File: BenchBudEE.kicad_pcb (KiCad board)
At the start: 4 copper layers, 165.1 x 63.5 mm, 54 parts, among them K1 1461069-5, P1 24-pin Mini-Fit Jr., P2 CONN_2, P3 CONN_3X2, P4 12-pin Terminal Block, P5 3-pin TB, Q1 2N3404, U1 LTV-816S, U10 LMT84, U11 OPA4170, U9 MCP3901

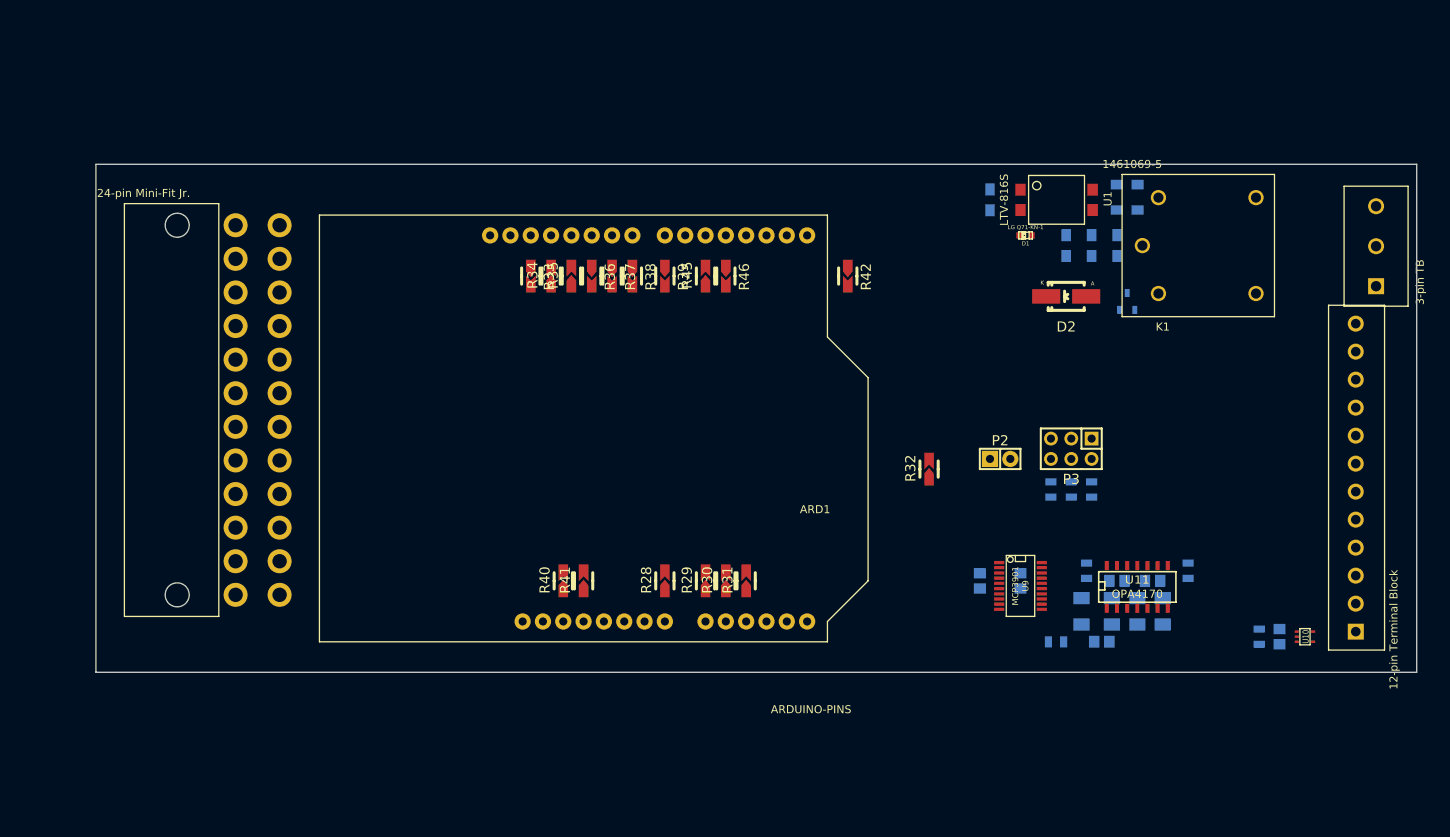
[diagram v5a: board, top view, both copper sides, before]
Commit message: Associated and placed the Current/Fan Driver Module
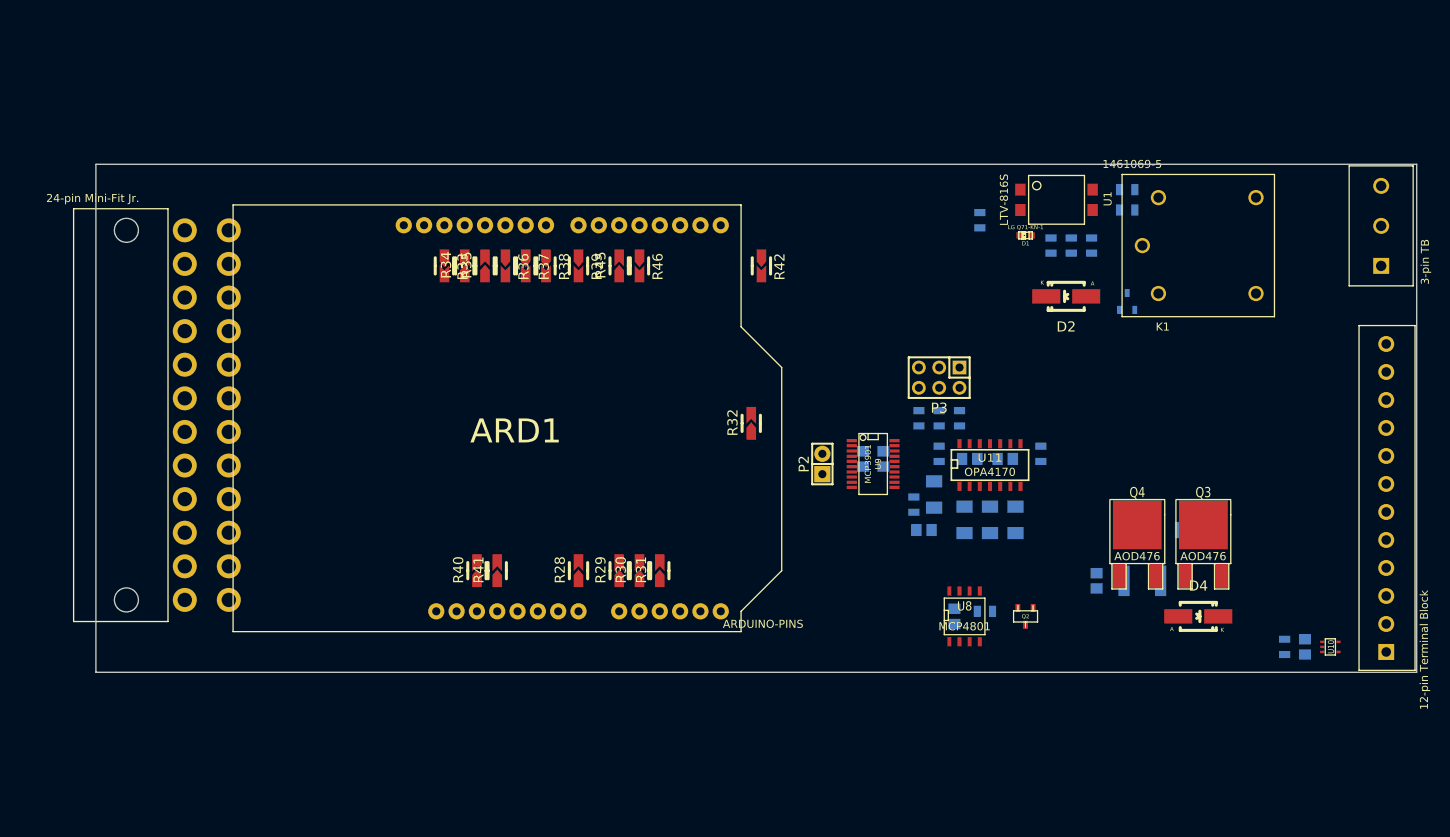
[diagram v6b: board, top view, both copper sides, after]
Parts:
- added C11: C, Capacitors_SMD:c_0805, B.Cu at (236.9, 168.3)
- added C12: C, Capacitors_SMD:c_0805, B.Cu at (254.6, 163.8)
- added D4: B130-13-F, Diodes_SMD:Diode-SMA_Handsoldering, F.Cu at (267.3, 168.3)
- added Q2: DMN65D8L-7, Transistors_SMD:sot23, F.Cu at (245.7, 168.3)
- added Q3: AOD476, SMD_Packages:DPAK2, F.Cu at (268.0, 163.2)
- added Q4: AOD476, SMD_Packages:DPAK2, F.Cu at (259.7, 163.2)
- added R19: R, SMD_Packages:SM0805, B.Cu at (240.7, 167.6)
- added R20: R, SMD_Packages:SM1206, B.Cu at (263.5, 157.5)
- added TH5: MINISMDC050F-2, SMD_Packages:SM1812, B.Cu at (260.4, 163.8)
- added U8: MCP4801, SMD_Packages:SO8N, F.Cu at (238.1, 168.3)
- R1, R2, R3, R4, R5, R6: footprint Resistors_SMD:Resistor_SMD0805_HandSoldering -> SMD_Packages:SM0805
- moved C7 26.3 mm to (233.0, 157.5)
- moved R48 24.7 mm to (231.8, 154.3), turned to 270 degrees
- moved R21 24.4 mm to (238.1, 156.2), turned to 90 degrees
- moved C8 23.9 mm to (238.8, 148.6)
- moved U9 23.9 mm to (226.7, 149.2)
- moved C9 23.9 mm to (243.2, 148.6)
- moved U11 23.9 mm to (241.3, 149.2)
- moved R27 23.5 mm to (234.9, 148.0)
- moved R22 23.5 mm to (234.3, 153.0), turned to 90 degrees
- moved R25 23.5 mm to (247.7, 148.0)
- moved R32 22.9 mm to (211.5, 144.1)
- moved C5 22.9 mm to (228.0, 148.6)
- moved P2 22.2 mm to (220.3, 149.2), turned to 90 degrees
- moved R23 21.7 mm to (244.5, 156.2)
- moved C6 21.1 mm to (225.4, 148.6)
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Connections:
- net /Arduino/ADC_CS_N renamed /Arduino/~ADC_CS
- ARD1 pad 27: (no net) -> Net-(ARD1-Pad27)
- ARD1 pad 28: (no net) -> Net-(ARD1-Pad28)

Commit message: Associated and placed the Power Filter Module
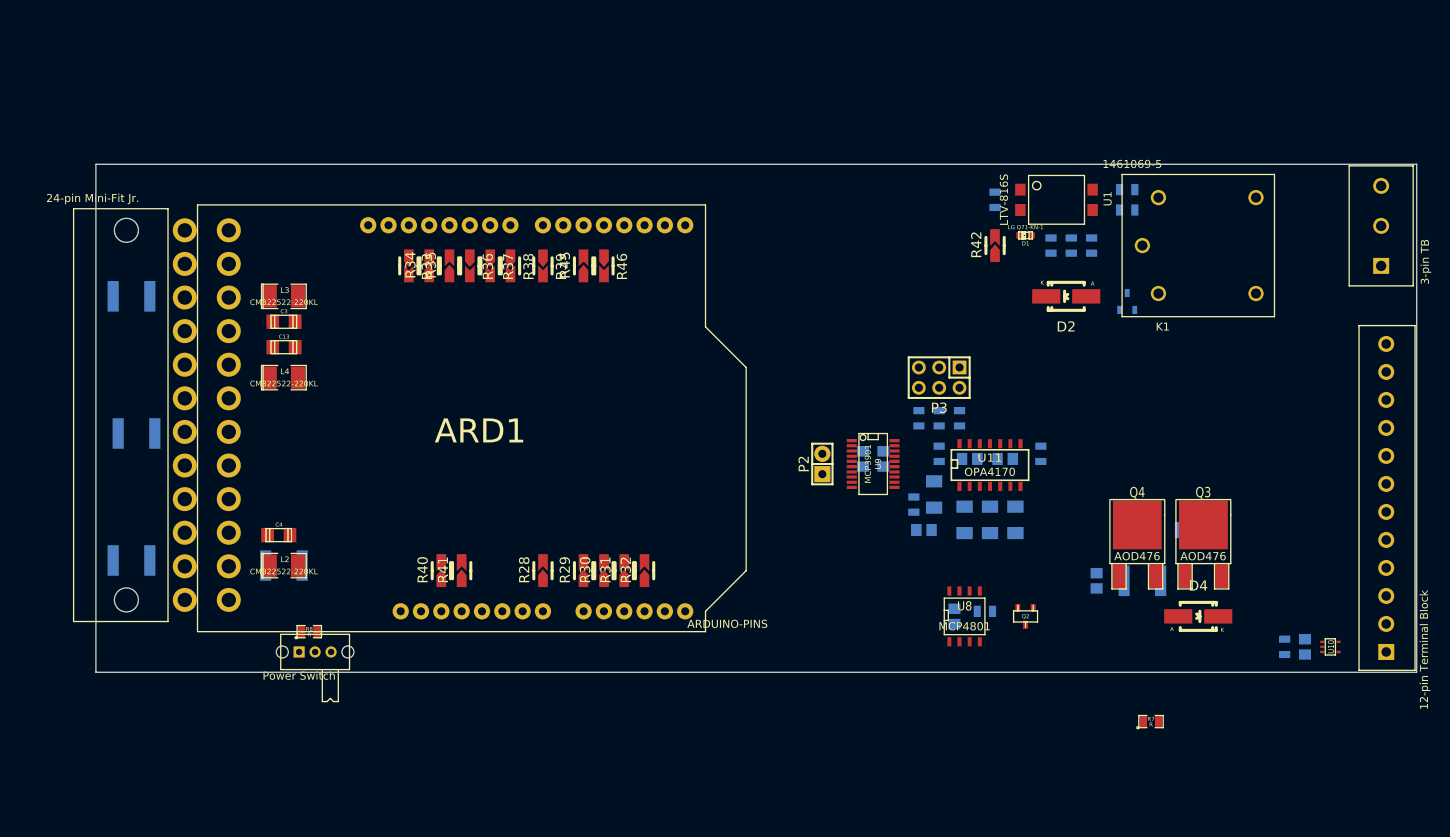
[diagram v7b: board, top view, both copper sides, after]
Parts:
- added C13: C, Capacitors_SMD:c_1206, F.Cu at (153.0, 134.6)
- added C3: C, Capacitors_SMD:c_1206, F.Cu at (153.0, 131.4)
- added C4: C, Capacitors_SMD:c_1206, F.Cu at (152.4, 158.1)
- added L2: CM322522-220KL, SMD_Packages:SM1210L, F.Cu at (153.0, 161.9)
- added L3: CM322522-220KL, SMD_Packages:SM1210L, F.Cu at (153.0, 128.3)
- added L4: CM322522-220KL, SMD_Packages:SM1210L, F.Cu at (153.0, 138.4)
- added R7: R, SMD_Packages:SM0805, F.Cu at (261.4, 181.4)
- added R8: R, SMD_Packages:SM0805, F.Cu at (156.2, 170.2)
- added SW1: Power Switch, BenchBudEE:BB_switch, F.Cu at (154.9, 172.7)
- added TH1: MINISMDC050F-2, SMD_Packages:SM1812, B.Cu at (134.0, 161.3)
- added TH2: MINISMDC050F-2, SMD_Packages:SM1812, B.Cu at (134.6, 145.4)
- added TH3: MINISMDC050F-2, SMD_Packages:SM1812, B.Cu at (134.0, 128.3)
- added TH4: MINISMDC050F-2, SMD_Packages:SM1812, B.Cu at (153.0, 161.9)
- moved R42 29.3 mm to (241.9, 121.9), turned to 90 degrees
- moved R32 22.7 mm to (198.1, 162.6)
- moved ARD1 4.45 mm to (203.2, 167.6)
- moved R28 4.45 mm to (185.4, 162.6)
- moved R30 4.45 mm to (193.0, 162.6)
- moved R35 4.45 mm to (173.7, 124.5)
- moved R39 4.45 mm to (185.4, 124.5)
- moved R41 4.45 mm to (175.3, 162.6)
- moved R46 4.45 mm to (193.0, 124.5)
- moved R29 4.44 mm to (190.5, 162.6)
- moved R31 4.44 mm to (195.6, 162.6)
- moved R33 4.44 mm to (168.7, 124.5)
- moved R34 4.44 mm to (171.2, 124.5)
- moved R36 4.44 mm to (176.3, 124.5)
- moved R37 4.44 mm to (178.8, 124.5)
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
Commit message: Associated and placed the Power Modification Module
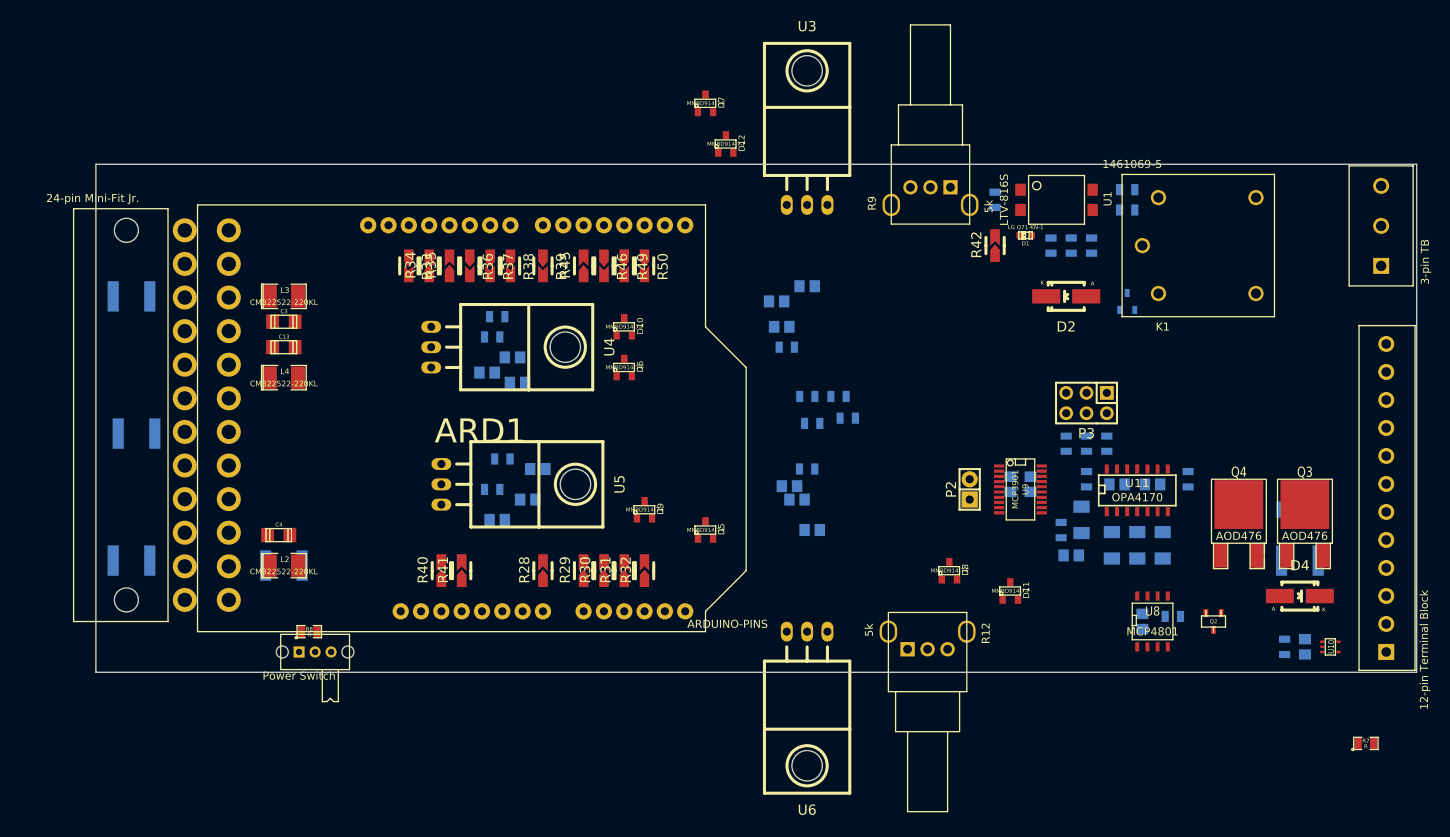
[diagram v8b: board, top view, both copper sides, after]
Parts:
- added C14: C, Capacitors_SMD:c_0805, B.Cu at (184.8, 149.9)
- added C15: C, Capacitors_SMD:c_0805, B.Cu at (215.3, 132.1)
- added C16: C, Capacitors_SMD:c_0805, B.Cu at (178.4, 137.8)
- added C17: C, Capacitors_SMD:c_0805, B.Cu at (219.1, 157.5)
- added C18: C, Capacitors_SMD:c_0805, B.Cu at (179.7, 156.2)
- added C19: C, Capacitors_SMD:c_0805, B.Cu at (181.6, 135.9)
- added C20: C, Capacitors_SMD:c_0805, B.Cu at (214.6, 128.9)
- added C21: C, Capacitors_SMD:c_0805, B.Cu at (217.2, 153.7)
- added C22: CP1, Capacitors_SMD:c_0805, B.Cu at (183.5, 153.7)
- added C23: CP1, Capacitors_SMD:c_0805, B.Cu at (182.2, 139.1)
- added C24: CP1, Capacitors_SMD:c_0805, B.Cu at (218.4, 127.0)
- added C25: CP1, Capacitors_SMD:c_0805, B.Cu at (216.2, 152.0)
- added D10: MMBD914-7-F, BenchBudEE:SOT23-DIODE, F.Cu at (195.6, 132.1)
- added D11: MMBD914-7-F, BenchBudEE:SOT23-DIODE, F.Cu at (243.8, 165.1)
- added D12: MMBD914-7-F, BenchBudEE:SOT23-DIODE, F.Cu at (208.3, 109.2)
- added D5: MMBD914-7-F, BenchBudEE:SOT23-DIODE, F.Cu at (205.7, 157.5)
- added D6: MMBD914-7-F, BenchBudEE:SOT23-DIODE, F.Cu at (195.6, 137.2)
- added D7: MMBD914-7-F, BenchBudEE:SOT23-DIODE, F.Cu at (205.7, 104.1)
- added D8: MMBD914-7-F, BenchBudEE:SOT23-DIODE, F.Cu at (236.2, 162.6)
- added D9: MMBD914-7-F, BenchBudEE:SOT23-DIODE, F.Cu at (198.1, 154.9)
- added R10: 680, SMD_Packages:SM0805, B.Cu at (215.9, 134.6)
- added R11: 680, SMD_Packages:SM0805, B.Cu at (218.4, 149.9)
- added R12: 5k, BenchBudEE:EVUE3K, F.Cu at (228.6, 170.2)
- added R15: R, SMD_Packages:SM0805, B.Cu at (218.5, 140.8)
- added R16: R, SMD_Packages:SM0805, B.Cu at (219.1, 144.1)
- added R17: R, SMD_Packages:SM0805, B.Cu at (222.4, 140.8)
- added R18: R, SMD_Packages:SM0805, B.Cu at (223.5, 143.5)
- added R49: R, BenchBudEE:Resistor_SMD0805_Blob, F.Cu at (195.6, 124.5)
- added R50: R, BenchBudEE:Resistor_SMD0805_Blob, F.Cu at (198.1, 124.5)
- added R51: R, SMD_Packages:SM0805, B.Cu at (179.1, 133.3)
- added R52: R, SMD_Packages:SM0805, B.Cu at (179.7, 130.8)
- added R53: R, SMD_Packages:SM0805, B.Cu at (180.3, 148.6)
- added R54: R, SMD_Packages:SM0805, B.Cu at (179.1, 152.4)
- added R9: 5k, BenchBudEE:EVUE3K, F.Cu at (238.8, 116.8)
- added U3: LM317T, Transistors_TO-220:TO-220_Neutral123_Horizontal, F.Cu at (218.4, 116.8)
- added U4: LM317T, Transistors_TO-220:TO-220_Neutral123_Horizontal, F.Cu at (171.4, 134.6)
- added U5: LM337T, Transistors_TO-220:TO-220_Neutral123_Horizontal, F.Cu at (172.7, 151.8)
- added U6: LM337T, Transistors_TO-220:TO-220_Neutral123_Horizontal, F.Cu at (218.4, 170.2)
- moved R7 27.0 mm to (288.3, 184.2)
- moved C11 23.5 mm to (260.4, 168.9)
- moved R19 23.5 mm to (264.2, 168.3)
- moved Q2 23.5 mm to (269.2, 168.9)
- moved U8 23.5 mm to (261.6, 168.9)
- moved C12 20.6 mm to (275.0, 160.7)
- moved TH5 19.8 mm to (280.0, 161.3)
- moved C7 18.7 mm to (251.5, 160.7)
- moved R43 18.7 mm to (253.4, 146.7)
- moved U9 18.7 mm to (245.1, 152.4)
- moved C8 18.7 mm to (257.2, 151.8)
- moved P3 18.7 mm to (253.4, 141.6)
- moved R21 18.7 mm to (256.5, 159.4)
- moved R27 18.7 mm to (253.4, 151.1)
- moved P2 18.7 mm to (238.8, 152.4)
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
